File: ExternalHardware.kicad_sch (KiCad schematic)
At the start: 7 parts, among them U6 74AHC74, U7 74AHC74, U8 GAL16V8

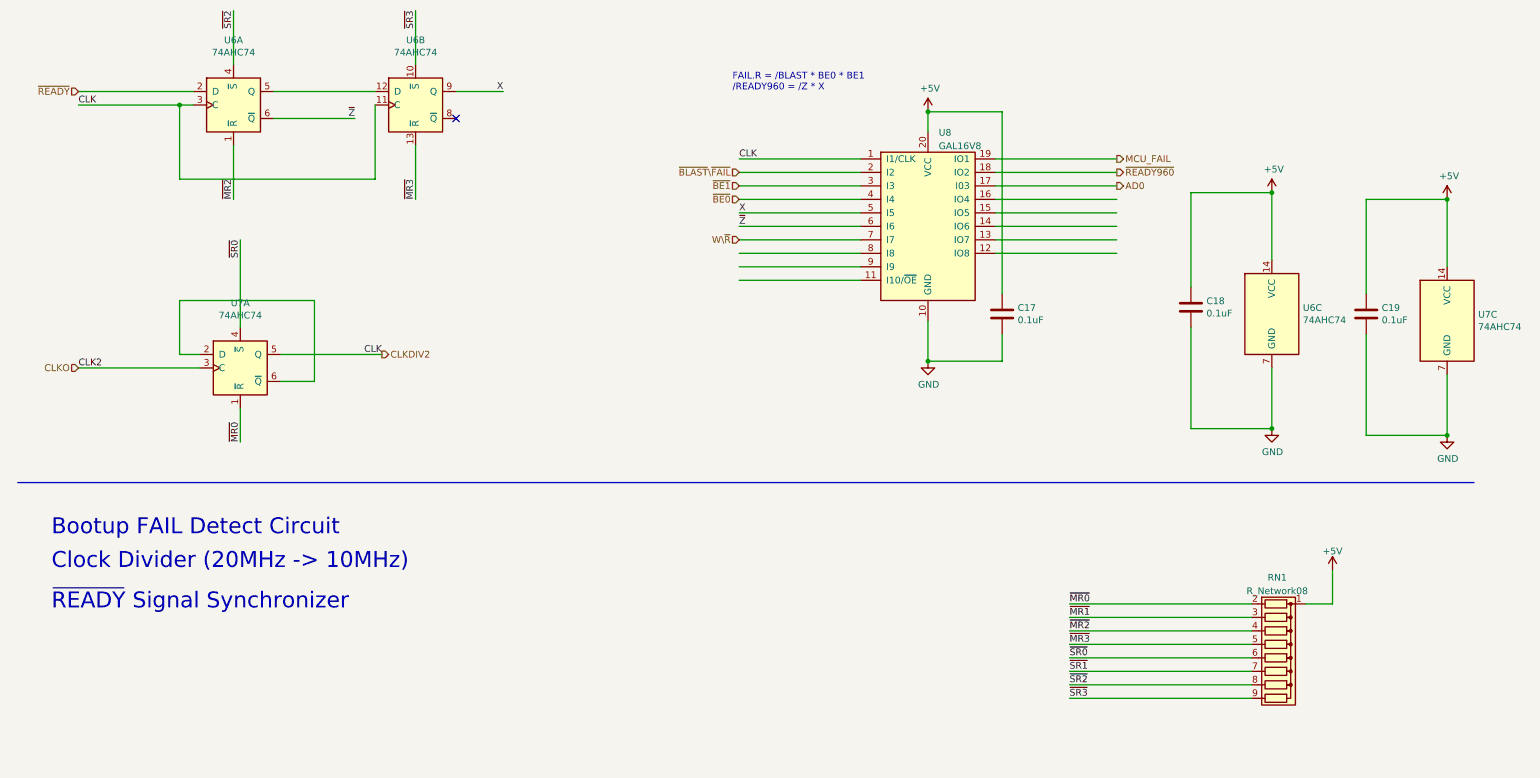
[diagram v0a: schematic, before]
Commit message: Use PLCC20 for the GAL chip instead of the much larger DIP20
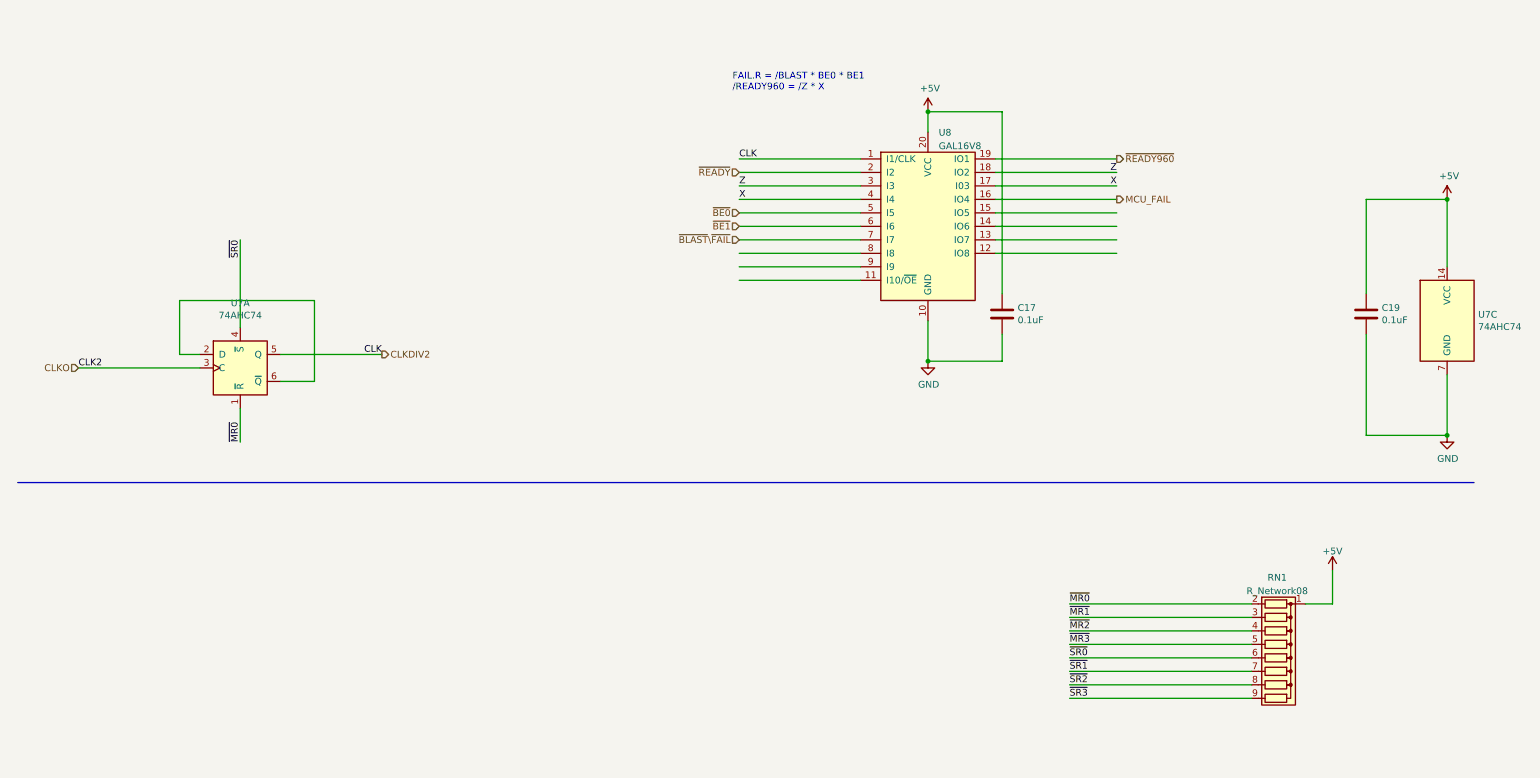
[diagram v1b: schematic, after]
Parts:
- removed C18: 0.1uF, Capacitor_THT:C_Disc_D5.0mm_W2.5mm_P2.50mm, symbol Device:C
- removed U6: 74AHC74, Package_SO:SOIC-14_3.9x8.7mm_P1.27mm, symbol 74xx:74HC74
- U8: footprint Package_DIP:DIP-20_W7.62mm_Socket -> Package_LCC:PLCC-20_THT-Socket
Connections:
- net AD0 is gone; now on net X: U8.17 (I03)
- net W\~{R} is gone; now on net ~{BLAST}\~{FAIL}: U8.7 (I7)
- net ~{Z} is gone; now on net ~{BE1}: U8.6 (I6)
- net MCU_FAIL: now also U8.16 (IO4); no longer U8.19 (IO1)
- net X: now also U8.4 (I4); no longer U8.5 (I5)
- net ~{BE0}: now also U8.5 (I5); no longer U8.4 (I4)
- net ~{BE1}: no longer U8.3 (I3)
- net ~{BLAST}\~{FAIL}: no longer U8.2 (I2)
- net ~{READY960}: now also U8.19 (IO1); no longer U8.18 (IO2)
- net ~{READY}: now also U8.2 (I2)
- new net Z: U8.18 (IO2), U8.3 (I3)
- no-connect marks 1 -> 0
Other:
- note removed: "Bootup FAIL Detect Circuit"
- note removed: "Clock Divider (20MHz -> 10MHz)"
- note removed: "~{READY} Signal Synchronizer"

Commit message: Introduce the 74LVC16T245 for the datalines
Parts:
- C19: footprint Capacitor_THT:C_Disc_D5.0mm_W2.5mm_P2.50mm -> Capacitor_SMD:C_0805_2012Metric_Pad1.18x1.45mm_HandSolder
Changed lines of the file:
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@@
       (effects (font (size 1.27 1.27)) (justify left))
     )
-    (property "Footprint" "Capacitor_THT:C_Disc_D5.0mm_W2.5mm_P2.50mm" (id 2) (at 266.3952 80.01 0)
+    (property "Footprint" "Capacitor_SMD:C_0805_2012Metric_Pad1.18x1.45mm_HandSolder" (id 2) (at 266.3952 80.01 0)
       (effects (font (size 1.27 1.27)) hide)
     )

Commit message: Just do the consolidation
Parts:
- removed RN1: R_Network08, Resistor_THT:R_Array_SIP9, symbol Device:R_Network08
- added R5, R6: 10k, Resistor_SMD:R_0805_2012Metric_Pad1.20x1.40mm_HandSolder, symbol Device:R
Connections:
- net +5V: now also R5.1, R6.1
- net ~{MR0}: now also R5.2
- net ~{SR0}: now also R6.2
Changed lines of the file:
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@@
+    (stroke (width 0) (type default) (color 0 0 0 0))
+  )
+  (wire (pts (xy 57.15 144.78) (xy 57.15 138.43))
     (stroke (width 0) (type default) (color 0 0 0 0))
   )
@@
     (stroke (width 0) (type default) (color 0 0 0 0))
   )
-  (wire (pts (xy 254 130.81) (xy 259.08 130.81))
-    (stroke (width 0) (type default) (color 0 0 0 0))
-  )
   (wire (pts (xy 147.32 46.99) (xy 170.18 46.99))
     (stroke (width 0) (type default) (color 0 0 0 0))
   )
-  (wire (pts (xy 209.55 133.35) (xy 243.84 133.35))
+  (wire (pts (xy 57.15 161.29) (xy 74.93 161.29))
+    (stroke (width 0) (type default) (color 0 0 0 0))
+  )
+  (wire (pts (xy 57.15 152.4) (xy 57.15 161.29))
     (stroke (width 0) (type default) (color 0 0 0 0))
   )
@@
     (stroke (width 0) (type default) (color 0 0 0 0))
   )
-  (wire (pts (xy 209.55 138.43) (xy 243.84 138.43))
-    (stroke (width 0) (type default) (color 0 0 0 0))
-  )
   (wire (pts (xy 147.32 62.23) (xy 170.18 62.23))
     (stroke (width 0) (type default) (color 0 0 0 0))
@@
     (stroke (width 0) (type default) (color 0 0 0 0))
   )
+  (wire (pts (xy 90.17 128.27) (xy 90.17 121.92))
+    (stroke (width 0) (type default) (color 0 0 0 0))
+  )
   (wire (pts (xy 195.58 57.15) (xy 218.44 57.15))
     (stroke (width 0) (type default) (color 0 0 0 0))
@@
     (stroke (width 0) (type default) (color 0 0 0 0))
   )
-  (wire (pts (xy 209.55 130.81) (xy 243.84 130.81))
-    (stroke (width 0) (type default) (color 0 0 0 0))
-  )
   (wire (pts (xy 147.32 59.69) (xy 170.18 59.69))
     (stroke (width 0) (type default) (color 0 0 0 0))
@@
     (stroke (width 0) (type default) (color 0 0 0 0))
   )
-  (wire (pts (xy 209.55 140.97) (xy 243.84 140.97))
-    (stroke (width 0) (type default) (color 0 0 0 0))
-  )
   (wire (pts (xy 280.67 99.06) (xy 280.67 87.63))
     (stroke (width 0) (type default) (color 0 0 0 0))
@@
     (stroke (width 0) (type default) (color 0 0 0 0))
   )
-  (wire (pts (xy 209.55 143.51) (xy 243.84 143.51))
-    (stroke (width 0) (type default) (color 0 0 0 0))
-  )
-  (wire (pts (xy 259.08 124.46) (xy 259.08 130.81))
+  (wire (pts (xy 90.17 144.78) (xy 107.95 144.78))
     (stroke (width 0) (type default) (color 0 0 0 0))
   )
@@
     (stroke (width 0) (type default) (color 0 0 0 0))
   )
-  (wire (pts (xy 209.55 135.89) (xy 243.84 135.89))
+  (wire (pts (xy 90.17 135.89) (xy 90.17 144.78))
     (stroke (width 0) (type default) (color 0 0 0 0))
   )
@@
     (stroke (width 0) (type default) (color 0 0 0 0))
   )
-  (wire (pts (xy 209.55 146.05) (xy 243.84 146.05))
-    (stroke (width 0) (type default) (color 0 0 0 0))
-  )
   (wire (pts (xy 195.58 49.53) (xy 218.44 49.53))
     (stroke (width 0) (type default) (color 0 0 0 0))
@@
     (stroke (width 0) (type default) (color 0 0 0 0))
   )
-  (wire (pts (xy 209.55 148.59) (xy 243.84 148.59))
-    (stroke (width 0) (type default) (color 0 0 0 0))
-  )
   (wire (pts (xy 265.43 80.01) (xy 265.43 99.06))
     (stroke (width 0) (type default) (color 0 0 0 0))
@@
     (effects (font (size 1.27 1.27)) (justify left bottom))
   )
-  (label "~{MR0}" (at 209.55 130.81 0)
-    (effects (font (size 1.27 1.27)) (justify left bottom))
+  (label "~{SR0}" (at 107.95 144.78 180)
+    (effects (font (size 1.27 1.27)) (justify right bottom))
   )
   (label "CLK2" (at 22.86 86.36 0)
     (effects (font (size 1.27 1.27)) (justify left bottom))
   )
-  (label "~{MR3}" (at 209.55 138.43 0)
-    (effects (font (size 1.27 1.27)) (justify left bottom))
-  )
-  (label "~{SR2}" (at 209.55 146.05 0)
-    (effects (font (size 1.27 1.27)) (justify left bottom))
-  )
   (label "Z" (at 147.32 52.07 0)
     (effects (font (size 1.27 1.27)) (justify left bottom))
   )
-  (label "~{SR0}" (at 209.55 140.97 0)
-    (effects (font (size 1.27 1.27)) (justify left bottom))
-  )
-  (label "~{SR1}" (at 209.55 143.51 0)
-    (effects (font (size 1.27 1.27)) (justify left bottom))
-  )
-  (label "~{MR2}" (at 209.55 135.89 0)
-    (effects (font (size 1.27 1.27)) (justify left bottom))
-  )
   (label "CLK" (at 147.32 46.99 0)
     (effects (font (size 1.27 1.27)) (justify left bottom))
@@
     (effects (font (size 1.27 1.27)) (justify right bottom))
   )
-  (label "~{MR1}" (at 209.55 133.35 0)
-    (effects (font (size 1.27 1.27)) (justify left bottom))
-  )
   (label "CLK" (at 80.01 83.82 180)
     (effects (font (size 1.27 1.27)) (justify right bottom))
@@
     (effects (font (size 1.27 1.27)) (justify left bottom))
   )
-  (label "~{SR3}" (at 209.55 148.59 0)
-    (effects (font (size 1.27 1.27)) (justify left bottom))
+  (label "~{MR0}" (at 74.93 161.29 180)
+    (effects (font (size 1.27 1.27)) (justify right bottom))
   )
   (hierarchical_label "~{READY960}" (shape output) (at 218.44 46.99 0)
@@
   (hierarchical_label "~{READY}" (shape input) (at 147.32 49.53 180)
     (effects (font (size 1.2954 1.2954)) (justify right))
-  )
-  (symbol (lib_id "Device:R_Network08") (at 248.92 140.97 270) (unit 1)
-    (in_bom yes) (on_board yes) (fields_autoplaced)
-    (property "Reference" "RN1" (id 0) (at 248.666 125.8402 90))
-    (property "Value" "R_Network08" (id 1) (at 248.666 128.3771 90))
-    (property "Footprint" "Resistor_THT:R_Array_SIP9" (id 2) (at 248.92 153.035 90)
-      (effects (font (size 1.27 1.27)) hide)
-    )
-    (property "Datasheet" "http://www.vishay.com/docs/31509/csc.pdf" (id 3) (at 248.92 140.97 0)
-      (effects (font (size 1.27 1.27)) hide)
-    )
-    (pin "1")
-    (pin "2")
-    (pin "3")
-    (pin "4")
-    (pin "5")
-    (pin "6")
-    (pin "7")
-    (pin "8")
-    (pin "9")
   )
   (symbol (lib_id "power:+5V") (at 280.67 54.61 0) (unit 1)
@@
     (pin "7")
   )
+  (symbol (lib_id "power:+5V") (at 90.17 121.92 0) (unit 1)
+    (in_bom yes) (on_board yes)
+    (property "Reference" "#PWR045" (id 0) (at 90.17 125.73 0)
+      (effects (font (size 1.27 1.27)) hide)
+    )
+    (property "Value" "+5V" (id 1) (at 90.551 117.5258 0))
+    (property "Footprint" "" (id 2) (at 90.17 121.92 0)
+      (effects (font (size 1.27 1.27)) hide)
+    )
+    (property "Datasheet" "" (id 3) (at 90.17 121.92 0)
+      (effects (font (size 1.27 1.27)) hide)
+    )
+    (pin "1")
+  )
   (symbol (lib_id "74xx:74HC74") (at 53.34 86.36 0) (unit 1)
     (in_bom yes) (on_board yes)
@@
     (pin "7")
   )
+  (symbol (lib_id "power:+5V") (at 57.15 138.43 0) (unit 1)
+    (in_bom yes) (on_board yes)
+    (property "Reference" "#PWR027" (id 0) (at 57.15 142.24 0)
+      (effects (font (size 1.27 1.27)) hide)
+    )
+    (property "Value" "+5V" (id 1) (at 57.531 134.0358 0))
+    (property "Footprint" "" (id 2) (at 57.15 138.43 0)
+      (effects (font (size 1.27 1.27)) hide)
+    )
+    (property "Datasheet" "" (id 3) (at 57.15 138.43 0)
+      (effects (font (size 1.27 1.27)) hide)
+    )
+    (pin "1")
+  )
   (symbol (lib_id "Device:C") (at 196.85 76.2 0) (unit 1)
     (in_bom yes) (on_board yes)
@@
     (pin "1")
   )
-  (symbol (lib_id "power:+5V") (at 259.08 124.46 0) (unit 1)
-    (in_bom yes) (on_board yes) (fields_autoplaced)
-    (property "Reference" "#PWR027" (id 0) (at 259.08 128.27 0)
-      (effects (font (size 1.27 1.27)) hide)
-    )
-    (property "Value" "+5V" (id 1) (at 259.08 120.8842 0))
-    (property "Footprint" "" (id 2) (at 259.08 124.46 0)
-      (effects (font (size 1.27 1.27)) hide)
-    )
-    (property "Datasheet" "" (id 3) (at 259.08 124.46 0)
-      (effects (font (size 1.27 1.27)) hide)
-    )
-    (pin "1")
-  )
   (symbol (lib_id "power:GND") (at 182.88 85.09 0) (unit 1)
     (in_bom yes) (on_board yes)
@@
     (pin "1")
   )
+  (symbol (lib_id "Device:R") (at 90.17 132.08 0) (unit 1)
+    (in_bom yes) (on_board yes)
+    (property "Reference" "R6" (id 0) (at 91.948 130.9116 0)
+      (effects (font (size 1.27 1.27)) (justify left))
+    )
+    (property "Value" "10k" (id 1) (at 91.948 133.223 0)
+      (effects (font (size 1.27 1.27)) (justify left))
+    )
+    (property "Footprint" "Resistor_SMD:R_0805_2012Metric_Pad1.20x1.40mm_HandSolder" (id 2) (at 88.392 132.08 90)
+      (effects (font (size 1.27 1.27)) hide)
+    )
+    (property "Datasheet" "~" (id 3) (at 90.17 132.08 0)
+      (effects (font (size 1.27 1.27)) hide)
+    )
+    (pin "1")
+    (pin "2")
+  )
+  (symbol (lib_id "Device:R") (at 57.15 148.59 0) (unit 1)
+    (in_bom yes) (on_board yes)
+    (property "Reference" "R5" (id 0) (at 58.928 147.4216 0)
+      (effects (font (size 1.27 1.27)) (justify left))
+    )
+    (property "Value" "10k" (id 1) (at 58.928 149.733 0)
+      (effects (font (size 1.27 1.27)) (justify left))
+    )
+    (property "Footprint" "Resistor_SMD:R_0805_2012Metric_Pad1.20x1.40mm_HandSolder" (id 2) (at 55.372 148.59 90)
+      (effects (font (size 1.27 1.27)) hide)
+    )
+    (property "Datasheet" "~" (id 3) (at 57.15 148.59 0)
+      (effects (font (size 1.27 1.27)) hide)
+    )
+    (pin "1")
+    (pin "2")
+  )
   (symbol (lib_id "power:GND") (at 280.67 99.06 0) (unit 1)

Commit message: Remove a resistor and drop the 10MHz output clock
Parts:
- removed R5: 10k, Resistor_SMD:R_0805_2012Metric_Pad1.20x1.40mm_HandSolder, symbol Device:R
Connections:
- net ~{MR0} is gone; now on net ~{SR0}: U7.1 (~{R})
- net CLKDIV2 renamed CLK
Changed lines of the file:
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@@
-    (stroke (width 0) (type default) (color 0 0 0 0))
-  )
-  (wire (pts (xy 57.15 144.78) (xy 57.15 138.43))
     (stroke (width 0) (type default) (color 0 0 0 0))
   )
@@
     (stroke (width 0) (type default) (color 0 0 0 0))
   )
-  (wire (pts (xy 57.15 161.29) (xy 74.93 161.29))
-    (stroke (width 0) (type default) (color 0 0 0 0))
-  )
-  (wire (pts (xy 57.15 152.4) (xy 57.15 161.29))
-    (stroke (width 0) (type default) (color 0 0 0 0))
-  )
   (wire (pts (xy 182.88 41.91) (xy 182.88 38.1))
     (stroke (width 0) (type default) (color 0 0 0 0))
@@
     (effects (font (size 1.27 1.27)) (justify left bottom))
   )
+  (label "~{SR0}" (at 53.34 100.33 90)
+    (effects (font (size 1.27 1.27)) (justify left bottom))
+  )
   (label "Z" (at 147.32 52.07 0)
     (effects (font (size 1.27 1.27)) (justify left bottom))
@@
     (effects (font (size 1.27 1.27)) (justify right bottom))
   )
-  (label "~{MR0}" (at 53.34 100.33 90)
-    (effects (font (size 1.27 1.27)) (justify left bottom))
-  )
   (label "Z" (at 218.44 49.53 180)
     (effects (font (size 1.27 1.27)) (justify right bottom))
@@
   (label "X" (at 147.32 54.61 0)
     (effects (font (size 1.27 1.27)) (justify left bottom))
-  )
-  (label "~{MR0}" (at 74.93 161.29 180)
-    (effects (font (size 1.27 1.27)) (justify right bottom))
   )
   (hierarchical_label "~{READY960}" (shape output) (at 218.44 46.99 0)
@@
   (hierarchical_label "~{BE1}" (shape input) (at 147.32 59.69 180)
     (effects (font (size 1.27 1.27)) (justify right))
-  )
-  (hierarchical_label "CLKDIV2" (shape output) (at 80.01 83.82 0)
-    (effects (font (size 1.27 1.27)) (justify left))
   )
   (hierarchical_label "MCU_FAIL" (shape output) (at 218.44 54.61 0)
@@
     (pin "7")
   )
-  (symbol (lib_id "power:+5V") (at 57.15 138.43 0) (unit 1)
-    (in_bom yes) (on_board yes)
-    (property "Reference" "#PWR027" (id 0) (at 57.15 142.24 0)
-      (effects (font (size 1.27 1.27)) hide)
-    )
-    (property "Value" "+5V" (id 1) (at 57.531 134.0358 0))
-    (property "Footprint" "" (id 2) (at 57.15 138.43 0)
-      (effects (font (size 1.27 1.27)) hide)
-    )
-    (property "Datasheet" "" (id 3) (at 57.15 138.43 0)
-      (effects (font (size 1.27 1.27)) hide)
-    )
-    (pin "1")
-  )
   (symbol (lib_id "Device:C") (at 196.85 76.2 0) (unit 1)
     (in_bom yes) (on_board yes)
@@
       (effects (font (size 1.27 1.27)) hide)
     )
-    (pin "1")
-    (pin "2")
-  )
-  (symbol (lib_id "Device:R") (at 57.15 148.59 0) (unit 1)
-    (in_bom yes) (on_board yes)
-    (property "Reference" "R5" (id 0) (at 58.928 147.4216 0)
-      (effects (font (size 1.27 1.27)) (justify left))
-    )
-    (property "Value" "10k" (id 1) (at 58.928 149.733 0)
-      (effects (font (size 1.27 1.27)) (justify left))
-    )
-    (property "Footprint" "Resistor_SMD:R_0805_2012Metric_Pad1.20x1.40mm_HandSolder" (id 2) (at 55.372 148.59 90)
-      (effects (font (size 1.27 1.27)) hide)
-    )
-    (property "Datasheet" "~" (id 3) (at 57.15 148.59 0)
-      (effects (font (size 1.27 1.27)) hide)
-    )

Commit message: Broke the link
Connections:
- no-connect marks 0 -> 7
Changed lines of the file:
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@@
   (junction (at 280.67 99.06) (diameter 0) (color 0 0 0 0)
   )
+  (no_connect (at 218.44 64.77))
+  (no_connect (at 147.32 64.77))
+  (no_connect (at 218.44 62.23))
+  (no_connect (at 218.44 57.15))
+  (no_connect (at 147.32 69.85))
+  (no_connect (at 147.32 67.31))
+  (no_connect (at 218.44 59.69))
   (wire (pts (xy 147.32 54.61) (xy 170.18 54.61))
     (stroke (width 0) (type default) (color 0 0 0 0))
